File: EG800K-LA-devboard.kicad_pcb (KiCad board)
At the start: 4 copper layers, 35 x 36.5 mm, 45 parts, among them J1 U.FL-R-SMT_10_, J2 MICROQTJ, J3 Conn_01x09_Pin, Q1 DTC143ZUAT106, Q2 DTC143ZUAT106, Q3 AO3415, Q4 DTC143ZUAT106, Q5 DTC143ZUAT106, U1 EG800KEULC-I03-SNNSA, U2 TP4057

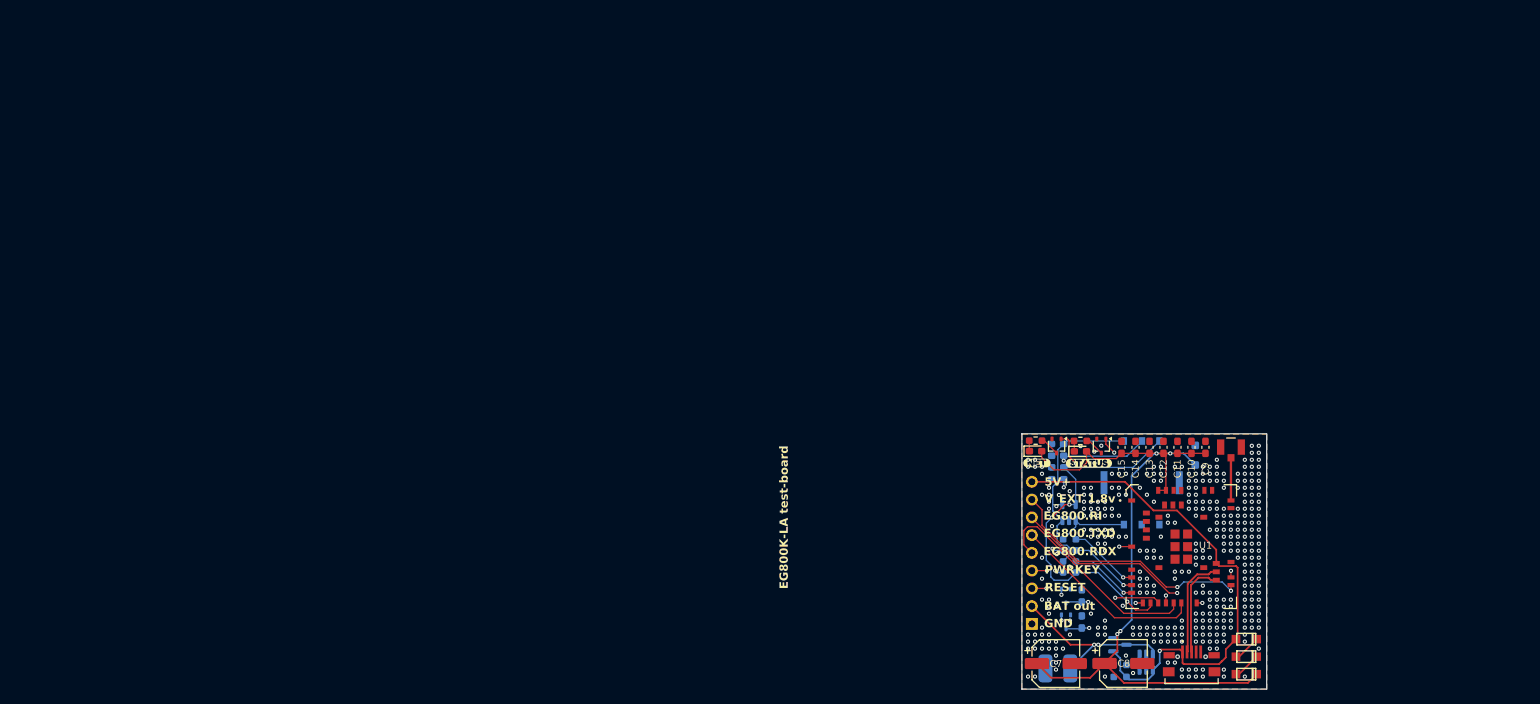
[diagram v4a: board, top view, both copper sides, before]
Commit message: agregado pin de vbat y detalles
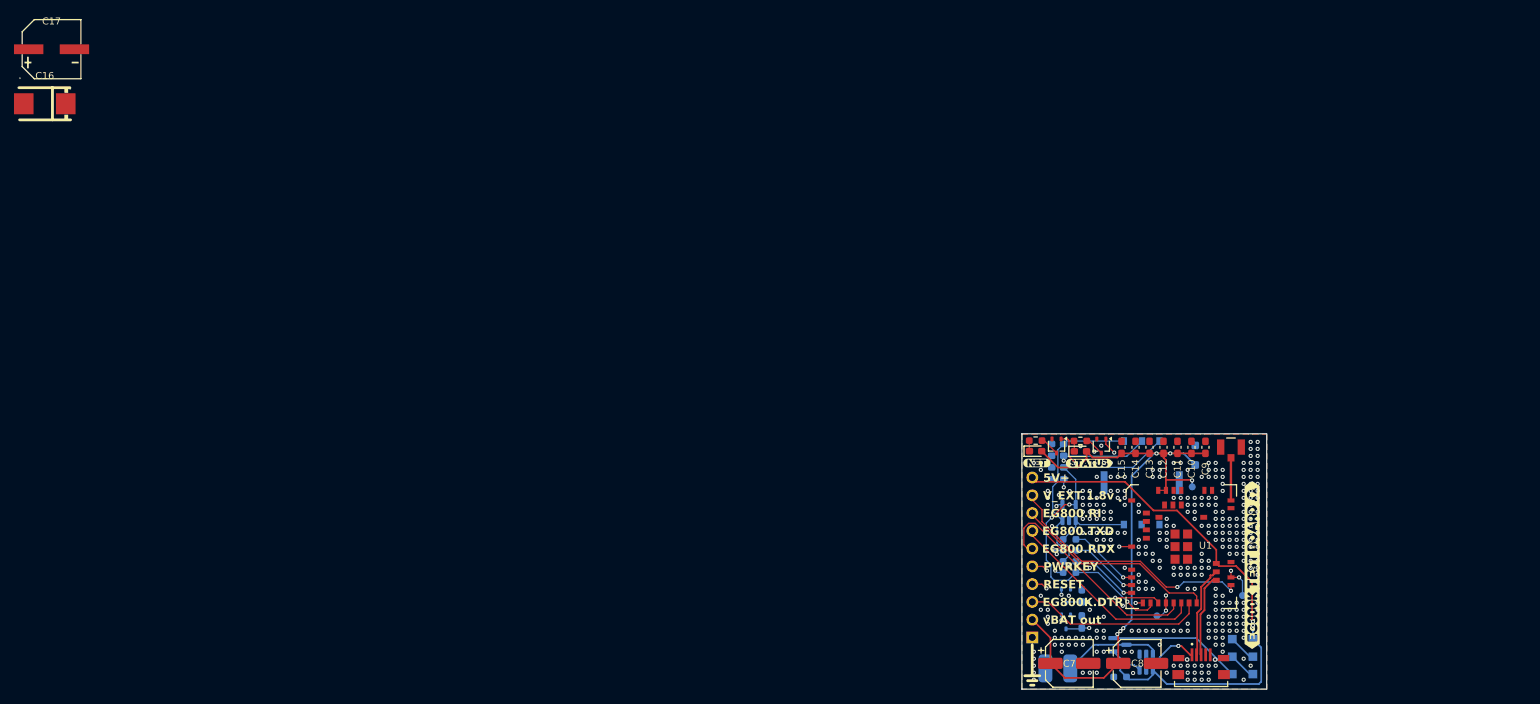
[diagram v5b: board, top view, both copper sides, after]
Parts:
- removed J3: Conn_01x09_Pin, Connector_PinHeader_2.54mm:PinHeader_1x09_P2.54mm_Vertical
- added ?: , , F.Cu at (168.0, 83.5)
- added C16: TAJD337K010RNJ, EasyEDA:CASE-D_7343, F.Cu at (4.40, 12.1)
- added C17: VT1A102M0810, EasyEDA:CAP-SMD_BD8.0-L8.3-W8.3-FD, F.Cu at (5.37, 4.30)
- added J4: Conn_01x11_Pin, Connector_PinHeader_2.54mm:PinHeader_1x10_P2.54mm_Vertical, B.Cu at (145.6, 88.4)
- added REF**: TestPoint_Pad_D1.0mm, TestPoint:TestPoint_Pad_D1.0mm, B.Cu at (168.5, 66.9)
- added REF**: TestPoint_Pad_D1.0mm, TestPoint:TestPoint_Pad_D1.0mm, B.Cu at (175.7, 82.4)
- added REF**: TestPoint_Pad_D1.0mm, TestPoint:TestPoint_Pad_D1.0mm, B.Cu at (163.4, 85.3)
- added kibuzzard-6A1B8E1D: G***, kibuzzard-6A1B8E1D, F.Cu at (177.0, 78.1)
- D2, D3, D4: moved to B.Cu
- moved C8 1.96 mm to (160.6, 92.1)
- moved C7 1.93 mm to (150.9, 92.1)
- moved J2 1.42 mm to (169.7, 91.6)
- moved D2 0.53 mm to (175.7, 88.7), turned to 0 degrees
- moved D3 0.53 mm to (175.7, 91.2), turned to 0 degrees
- moved D4 0.53 mm to (175.7, 93.7), turned to 0 degrees
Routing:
- net /EG800K.MAIN_DTR: track 0.00 -> 25.9 mm
- net +5V: track 73.4 -> 88.6 mm, vias 1 -> 4
- net +4.2V: track 25.9 -> 14.2 mm, vias 2 -> 0
- net /DC 3.8v supply: track 108.7 -> 116.1 mm, vias 4 -> 6
- net /EG800K.STATUS: track 27.2 -> 31.1 mm, vias 2 -> 3
- net /EG800K.NET_STATUS: track 30.2 -> 32.9 mm, vias 2 -> 3
- net /EG800K.USB_D+: track 13.9 -> 11.9 mm
- net /EG800K.USB_D-: track 14.7 -> 13.2 mm
- net /HOST.EG800K.PWRKEY: track 7.35 -> 8.20 mm
- net /EG800K.UART1_RXD: track 31.6 -> 32.4 mm
- net /EG800K.UART1_Ri: track 30.3 -> 30.2 mm, vias 2 -> 0
- net GND: vias 363 -> 327
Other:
- board text added: "EG800K.DTR"
- board text added: "T.1"
- board text added: "T.2"
- board text added: "T.3"
- board text added: "vBAT out"
- board text removed: "BAT out"
- board text removed: "EG800K-LA test-board"
- board text removed: "GND"
- board text removed: "tapered RF 0.3424 clear 0.5080 Coplanar Single Ended"

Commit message: carga final
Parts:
- removed BAT+1: BAT+, Connector_Wire:SolderWirePad_1x01_SMD_2x4mm
- removed BAT-1: BAT-, Connector_Wire:SolderWirePad_1x01_SMD_2x4mm
- removed C16: TAJD337K010RNJ, EasyEDA:CASE-D_7343
- removed C17: VT1A102M0810, EasyEDA:CAP-SMD_BD8.0-L8.3-W8.3-FD
- added CN1: 530480210, EasyEDA:CONN-TH_530480210, F.Cu at (176.7, 91.0)
- moved D4 9.55 mm to (176.4, 84.1)
- moved D3 4.99 mm to (176.4, 86.2)
- moved kibuzzard-6A1B8E1D 1.91 mm to (177.3, 76.2)
- moved D2 0.85 mm to (176.4, 88.3)
- moved REF** 0.79 mm to (175.7, 81.6)
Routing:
- net +4.2V: track 14.2 -> 19.8 mm
- net +5V: track 88.6 -> 90.3 mm, vias 4 -> 3
- net /EG800K.UART1_RXD: track 32.4 -> 33.5 mm
- net /EG800K.VDD_ETX: track 36.9 -> 35.9 mm
- net /EG800K.STATUS: track 31.1 -> 30.4 mm
- net GND: vias 327 -> 330

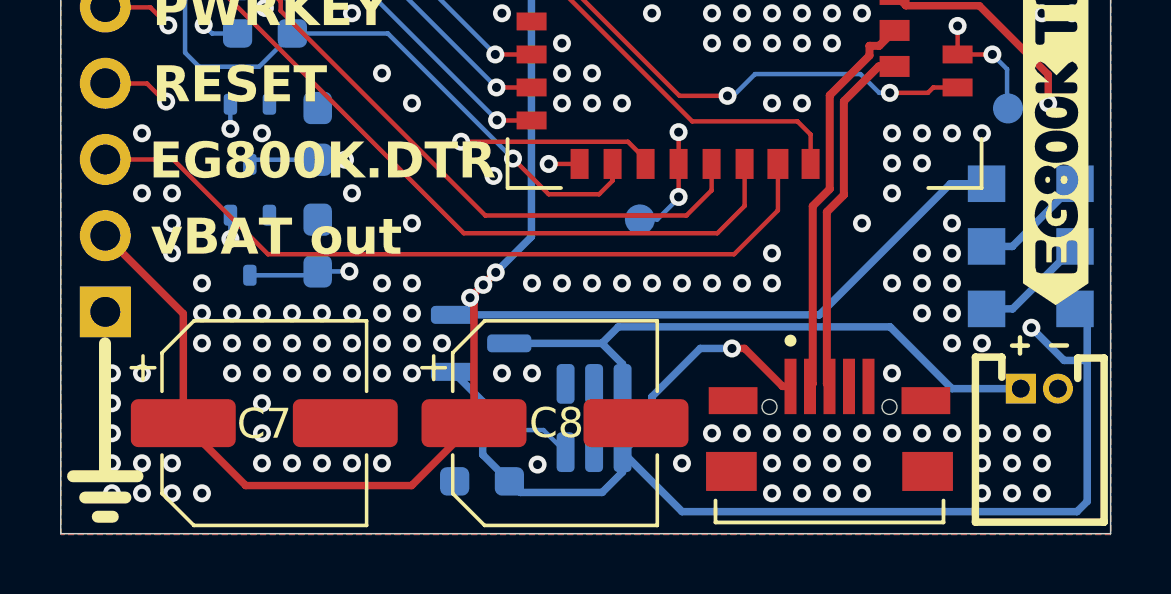
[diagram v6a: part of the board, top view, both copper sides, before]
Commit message: removido la etapa de carga de BAT
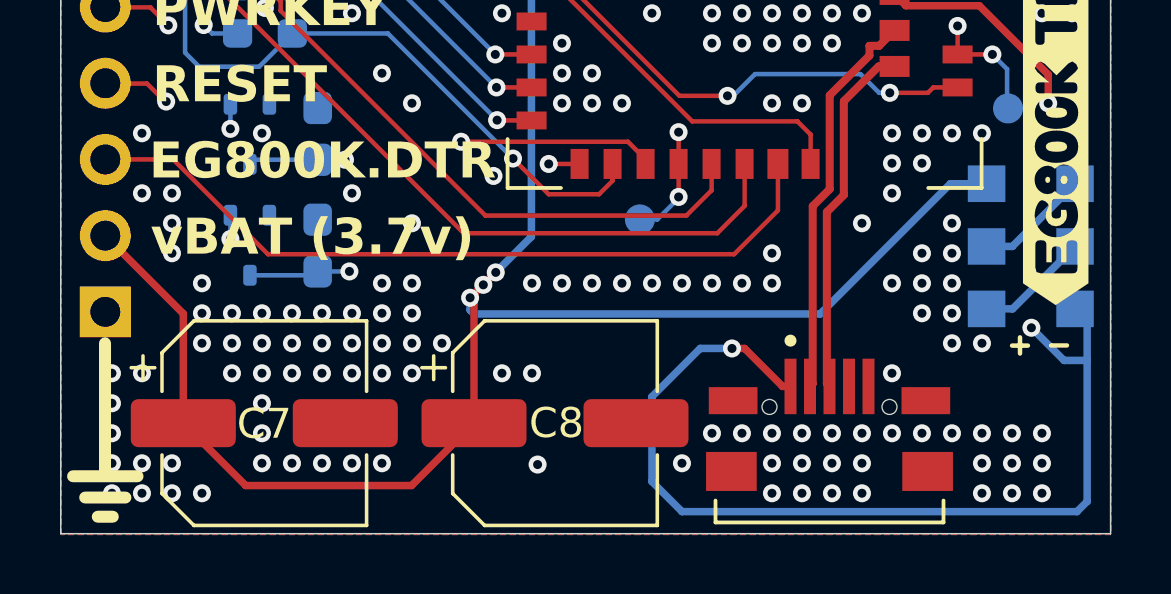
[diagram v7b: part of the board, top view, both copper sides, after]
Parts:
- removed CN1: 530480210, EasyEDA:CONN-TH_530480210
- removed Q3: AO3415, Package_TO_SOT_SMD:SOT-23
- removed R5: 2.4K, Resistor_SMD:R_0603_1608Metric_Pad0.98x0.95mm_HandSolder
- removed R6: 10k, Resistor_SMD:R_0603_1608Metric_Pad0.98x0.95mm_HandSolder
- removed U2: TP4057, Package_TO_SOT_SMD:TSOT-23-6
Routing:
- net +4.2V: track 19.8 -> 0.00 mm
- net +5V: track 90.3 -> 80.2 mm
- net Net-(U2-PROG): track 2.19 -> 0.00 mm
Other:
- board text added: "vBAT (3.7v)"
- board text removed: "vBAT out"

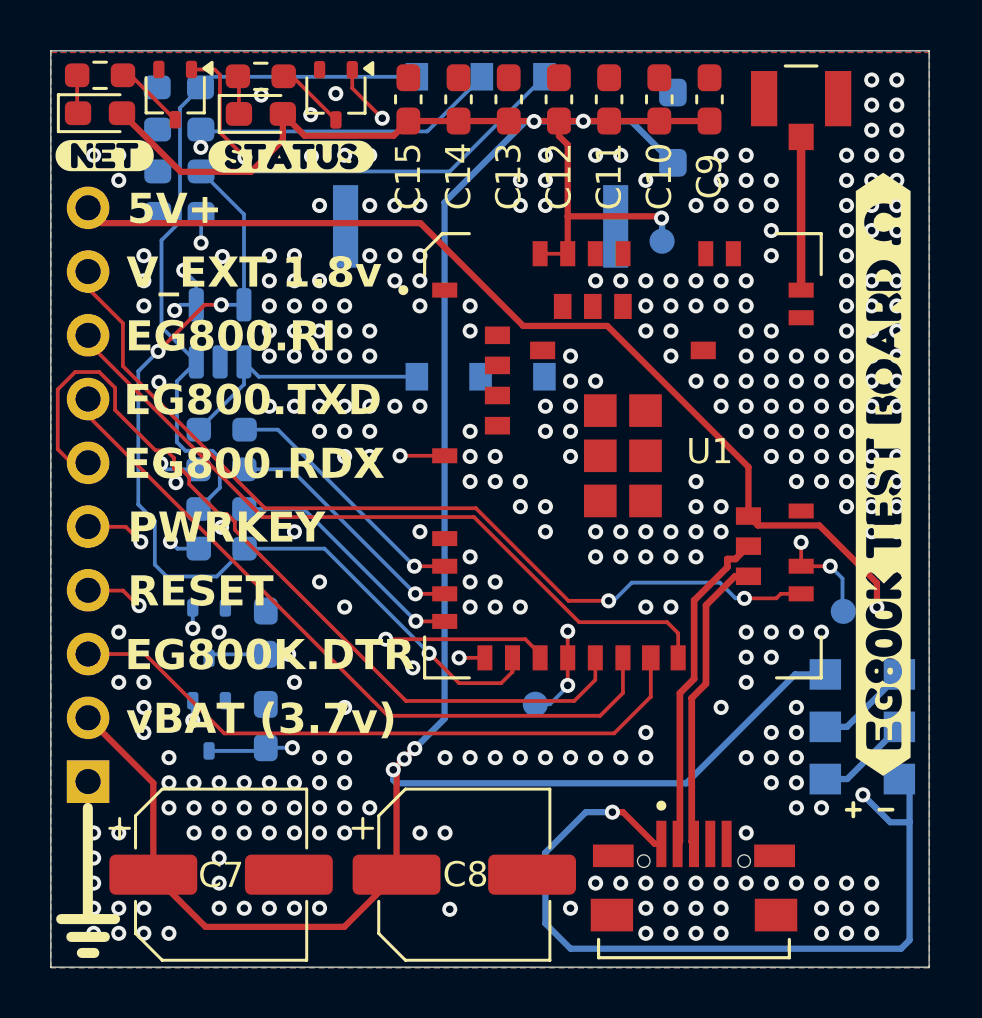
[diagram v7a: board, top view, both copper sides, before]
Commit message: Agregados res en serie en USB
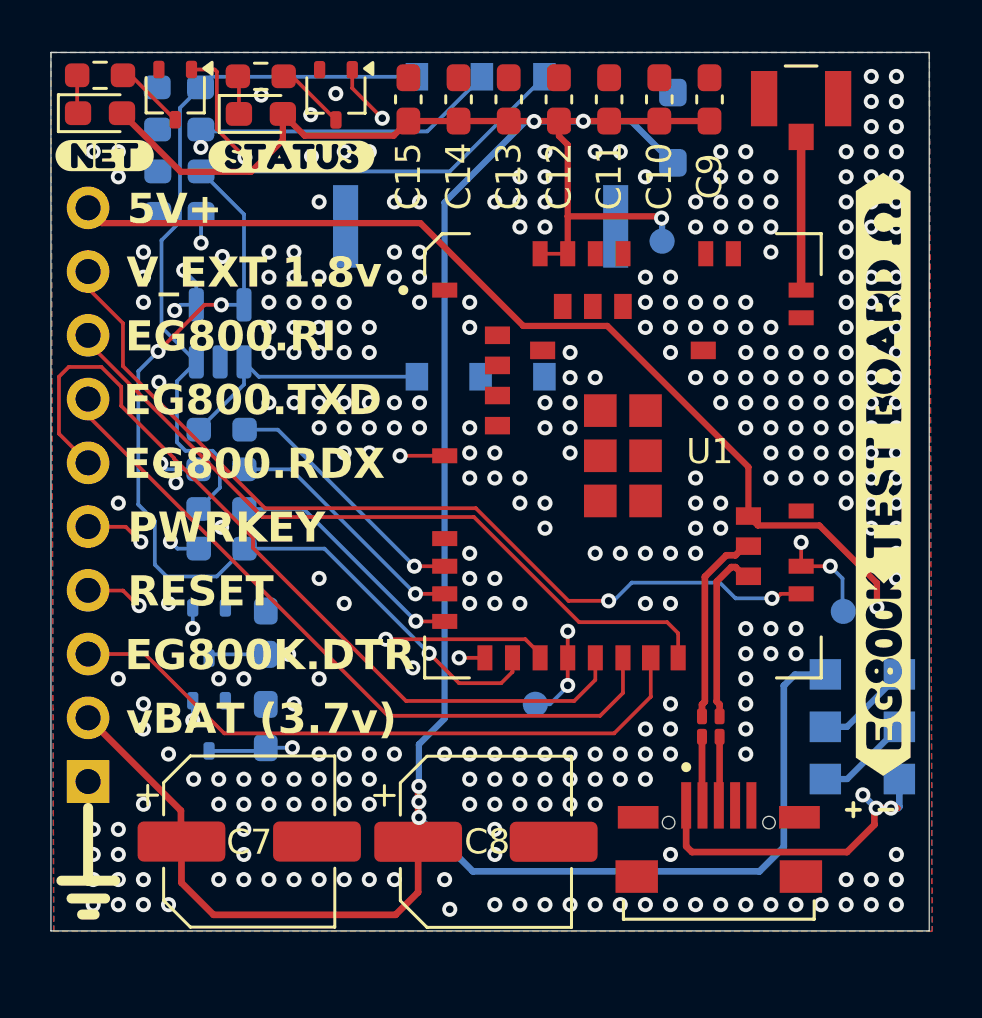
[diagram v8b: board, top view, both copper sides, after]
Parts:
- added R5: 22, Resistor_SMD:R_0201_0603Metric_Pad0.64x0.40mm_HandSolder, F.Cu at (170.1, 86.2)
- added R6: 22, Resistor_SMD:R_0201_0603Metric_Pad0.64x0.40mm_HandSolder, F.Cu at (170.8, 86.2)
- moved J2 1.83 mm to (170.7, 90.0)
- moved C7 1.73 mm to (152.0, 90.8)
- moved C8 1.57 mm to (161.4, 90.8)
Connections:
- J2 pad 2: /EG800K.USB_D- -> Net-(J2-D-)
- J2 pad 3: /EG800K.USB_D+ -> Net-(J2-D+)
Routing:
- net +5V: track 80.2 -> 62.1 mm, vias 3 -> 4
- net /EG800K.USB_D-: track 13.2 -> 7.85 mm
- net /EG800K.USB_D+: track 11.9 -> 7.07 mm
- net /DC 3.8v supply: track 116.5 -> 121.2 mm
- net Net-(J2-D+): track 0.00 -> 2.74 mm
- net Net-(J2-D-): track 0.00 -> 2.74 mm
- net /EG800K.UART1_RXD: track 33.5 -> 32.9 mm
- net GND: vias 330 -> 331
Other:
- board size 35 x 36.5 mm -> 35 x 35 mm
